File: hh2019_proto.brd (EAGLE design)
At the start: 250.5 x 149.7 mm, 145 parts, among them IC1 CP210X_USB_UART, IC2 AP2114H, IC4 TP4056, J1 PJ-313D, Q1 MMBT2222A, Q3 MMBT2222A, Q4 MMBT2222A, Q5 SI1304 BDL, U1 MPR121QR2, U2 ESP32-WROVER-I, U3 PCM5102A, X4 JST-PH3

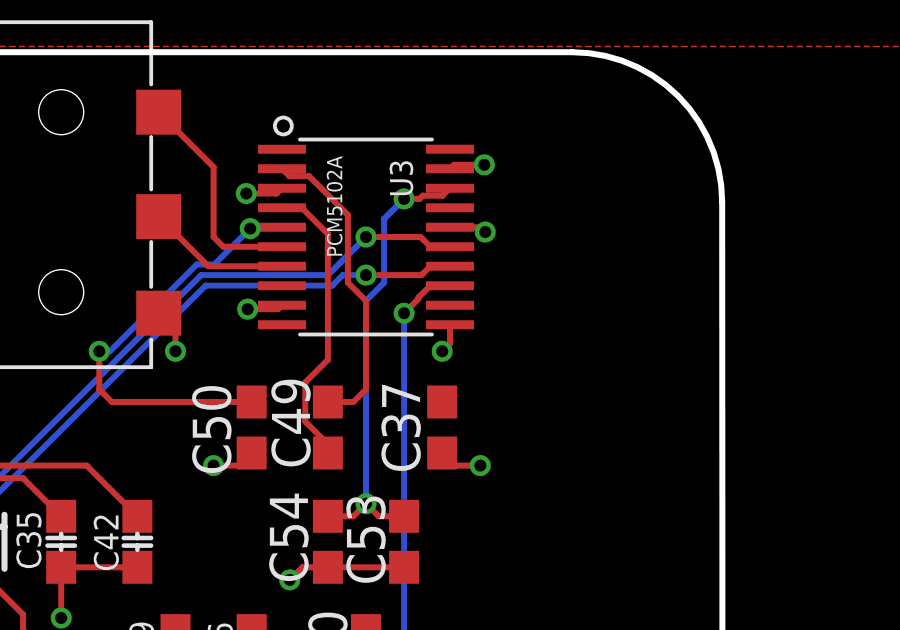
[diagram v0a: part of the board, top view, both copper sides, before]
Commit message: Fixed floating DAC pins being unconnected
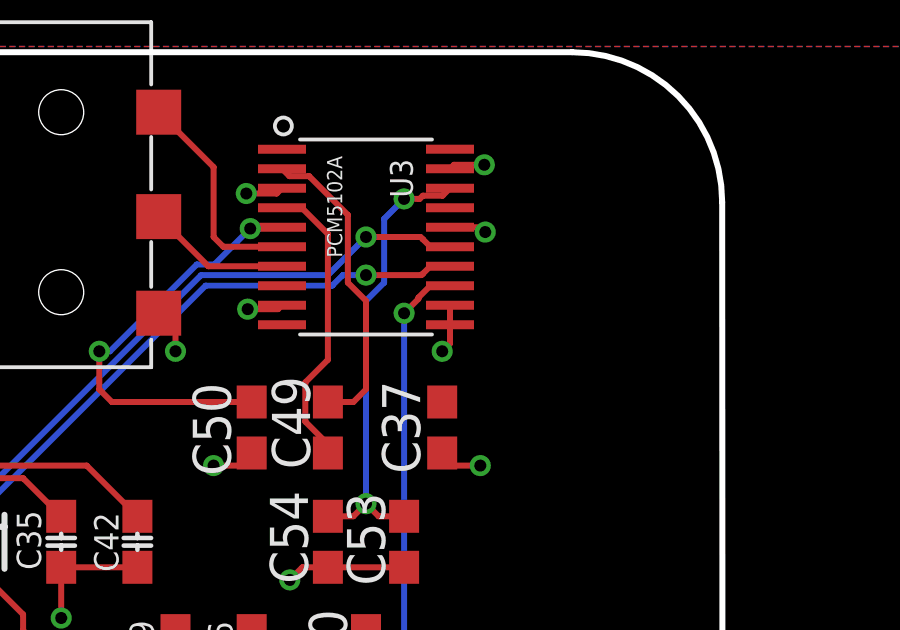
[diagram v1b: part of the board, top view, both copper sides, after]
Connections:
- removed net +3V3: U3.P$17
- removed net DEMP: U3.P$10
- net 3V3: now also U3.P$17
- net GND: now also U3.P$10
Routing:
- net GND: track 175.9 -> 176.6 mm
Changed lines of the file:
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@@
 <via x="-110.49" y="135.89" extent="1-16" drill="0.4"/>
 <contactref element="U3" pad="P$12"/>
+<wire x1="-93.72" y1="137.425" x2="-93.72" y2="136.775" width="0.2" layer="1"/>
+<contactref element="U3" pad="P$10"/>
 <wire x1="123.19" y1="72.39" x2="133.35" y2="72.39" width="0" layer="19" extent="1-1"/>
 <wire x1="114.3" y1="72.39" x2="123.19" y2="72.39" width="0" layer="19" extent="1-1"/>
@@
 <wire x1="104.14" y1="20.32" x2="114.3" y2="20.32" width="0" layer="19" extent="1-1"/>
 <wire x1="95.25" y1="20.32" x2="104.14" y2="20.32" width="0" layer="19" extent="1-1"/>
-<wire x1="-87.63" y1="68.58" x2="95.25" y2="72.39" width="0" layer="19" extent="1-1"/>
-<wire x1="-87.63" y1="76.2" x2="-87.63" y2="68.58" width="0" layer="19" extent="1-1"/>
-<wire x1="-87.593" y1="80.95" x2="-87.63" y2="76.2" width="0" layer="19" extent="1-1"/>
-<wire x1="-89.32" y1="86.36" x2="-88.9" y2="81.28" width="0" layer="19" extent="1-1"/>
-<wire x1="-87.593" y1="91.11" x2="-88.9" y2="87.63" width="0" layer="19" extent="1-1"/>
-<wire x1="-89.32" y1="96.52" x2="-88.9" y2="91.44" width="0" layer="19" extent="1-1"/>
-<wire x1="-87.593" y1="101.27" x2="-88.9" y2="97.79" width="0" layer="19" extent="1-1"/>
-<wire x1="-89.32" y1="106.68" x2="-88.9" y2="101.6" width="0" layer="19" extent="1-1"/>
-<wire x1="-96.47" y1="77.97" x2="-89.22" y2="76.2" width="0" layer="19" extent="1-1"/>
-<wire x1="-100.83" y1="78.77" x2="-99.06" y2="76.2" width="0" layer="19" extent="1-1"/>
-<wire x1="-100.4" y1="89.3" x2="-98.71" y2="86.44" width="0" layer="19" extent="1-1"/>
-<wire x1="-107.53" y1="90.17" x2="-102.84" y2="89.3" width="0" layer="19" extent="1-1"/>
-<wire x1="-113.88" y1="86.36" x2="-109.22" y2="90.17" width="0" layer="19" extent="1-1"/>
-<wire x1="-119.38" y1="91.44" x2="-113.88" y2="86.36" width="0" layer="19" extent="1-1"/>
-<wire x1="-99.06" y1="67.31" x2="-99.695" y2="75.565" width="0" layer="19" extent="1-1"/>
-<wire x1="-109.64" y1="63.5" x2="-99.06" y2="63.5" width="0" layer="19" extent="1-1"/>
-<wire x1="-114.046" y1="65.405" x2="-110.49" y2="64.77" width="0" layer="19" extent="1-1"/>
-<wire x1="-115.57" y1="57.47" x2="-110.04" y2="60.96" width="0" layer="19" extent="1-1"/>
-<wire x1="-118.11" y1="57.57" x2="-115.57" y2="57.47" width="0" layer="19" extent="1-1"/>
-<wire x1="-122.368240625" y1="49.15075625" x2="-118.11" y2="57.57" width="0" layer="19" extent="1-1"/>
-<wire x1="-118.91" y1="47.2" x2="-122.368240625" y2="49.15075625" width="0" layer="19" extent="1-1"/>
-<wire x1="-123.231115625" y1="42.646378125" x2="-123.49" y2="47.75" width="0" layer="19" extent="1-1"/>
-<wire x1="-124.206" y1="65.405" x2="-114.3" y2="65.659" width="0" layer="19" extent="1-1"/>
-<wire x1="-134.62" y1="98.21" x2="-123.16" y2="91.85" width="0" layer="19" extent="1-1"/>
-<wire x1="-140.34" y1="108.03" x2="-135.89" y2="98.21" width="0" layer="19" extent="1-1"/>
-<wire x1="-152.4" y1="107.95" x2="-140.34" y2="108.03" width="0" layer="19" extent="1-1"/>
-<wire x1="-152.4" y1="101.6" x2="-152.82" y2="106.68" width="0" layer="19" extent="1-1"/>
-<wire x1="-152.4" y1="97.79" x2="-151.093" y2="101.27" width="0" layer="19" extent="1-1"/>
-<wire x1="-152.4" y1="91.44" x2="-152.82" y2="96.52" width="0" layer="19" extent="1-1"/>
-<wire x1="-152.4" y1="87.63" x2="-151.093" y2="91.11" width="0" layer="19" extent="1-1"/>
-<wire x1="-152.4" y1="81.28" x2="-152.82" y2="86.36" width="0" layer="19" extent="1-1"/>
-<wire x1="-111.76" y1="108.827" x2="-111.76" y2="94.4" width="0" layer="19" extent="1-1"/>
-<wire x1="-122.56" y1="108.03" x2="-111.76" y2="108.827" width="0" layer="19" extent="1-1"/>
-<wire x1="-111.64" y1="121.92" x2="-110.49" y2="109.22" width="0" layer="19" extent="1-1"/>
-<wire x1="-110.49" y1="125.73" x2="-113.03" y2="123.61" width="0" layer="19" extent="1-1"/>
-<wire x1="-110.49" y1="128.4548" x2="-110.49" y2="125.73" width="0" layer="19" extent="1-1"/>
-<wire x1="-116.84" y1="128.69" x2="-114.3" y2="128.69" width="0" layer="19" extent="1-1"/>
-<wire x1="-106.68" y1="127" x2="-109.22" y2="124.88" width="0" layer="19" extent="1-1"/>
-<wire x1="-104.14" y1="124.46" x2="-106.68" y2="127" width="0" layer="19" extent="1-1"/>
-<wire x1="-99.06" y1="128.27" x2="-100.33" y2="124.88" width="0" layer="19" extent="1-1"/>
-<wire x1="-93.56" y1="132.08" x2="-95.25" y2="128.69" width="0" layer="19" extent="1-1"/>
-<wire x1="-93.98" y1="135.89" x2="-93.98" y2="132.5" width="0" layer="19" extent="1-1"/>
-<wire x1="-93.72" y1="137.425" x2="-93.72" y2="136.775" width="0" layer="19" extent="1-1"/>
-<wire x1="-93.72" y1="140.025" x2="-93.72" y2="137.425" width="0" layer="19" extent="1-1"/>
-<wire x1="-93.72" y1="141.975" x2="-93.72" y2="140.025" width="0" layer="19" extent="1-1"/>
-<wire x1="-100.75" y1="132.08" x2="-98.64" y2="128.69" width="0" layer="19" extent="1-1"/>
-<wire x1="-102.87" y1="135.89" x2="-101.6" y2="132.08" width="0" layer="19" extent="1-1"/>
-<wire x1="-100.464446875" y1="137.294446875" x2="-102.87" y2="136.6" width="0" layer="19" extent="1-1"/>
-<wire x1="-99.495553125" y1="141.149446875" x2="-99.32" y2="137.425" width="0" layer="19" extent="1-1"/>
-<wire x1="-102.87" y1="119.7" x2="-103.29" y2="124.46" width="0" layer="19" extent="1-1"/>
-<wire x1="-119.93" y1="133.99" x2="-119.38" y2="128.69" width="0" layer="19" extent="1-1"/>
-<wire x1="-124.43" y1="133.99" x2="-119.93" y2="133.99" width="0" layer="19" extent="1-1"/>
-<wire x1="-109.93" y1="137.16" x2="-103.43" y2="137.16" width="0" layer="19" extent="1-1"/>
-<wire x1="-133.9076" y1="132.60455" x2="-124.43" y2="133.99" width="0" layer="19" extent="1-1"/>
-<wire x1="-142.24" y1="128.69" x2="-137.16" y2="133.35" width="0" layer="19" extent="1-1"/>
-<wire x1="-146.05" y1="127.42" x2="-142.24" y2="128.69" width="0" layer="19" extent="1-1"/>
-<wire x1="-146.05" y1="139.58" x2="-146.05" y2="132.4" width="0" layer="19" extent="1-1"/>
-<wire x1="-142.24" y1="143.51" x2="-146.05" y2="140.97" width="0" layer="19" extent="1-1"/>
-<wire x1="-134.25" y1="141.89" x2="-138.05" y2="141.09" width="0" layer="19" extent="1-1"/>
+<wire x1="-87.63" y1="76.2" x2="95.25" y2="72.39" width="0" layer="19" extent="1-1"/>
+<wire x1="-99.32" y1="136.775" x2="-99.450553125" y2="137.294446875" width="0" layer="19" extent="1-1"/>
 </signal>
 <signal name="USB_DN_CON">
@@
 <wire x1="-112.71" y1="59.37" x2="-107.95" y2="54.61" width="0.2" layer="1"/>
 <wire x1="-107.95" y1="54.61" x2="-104.14" y2="54.61" width="0.2" layer="1"/>
+<contactref element="U3" pad="P$17"/>
 </signal>
 <signal name="GDR">
@@
 <wire x1="-104.99" y1="134.2" x2="-100.33" y2="134.2" width="0.2" layer="1"/>
 </signal>
-<signal name="DEMP" class="2">
-<contactref element="U3" pad="P$10"/>
-</signal>
 <signal name="BAT" class="1">
 <contactref element="X4" pad="3"/>
@@
 <wire x1="-106.045" y1="76.835" x2="-107.175" y2="76.835" width="0.2" layer="1"/>
 </signal>
-<signal name="+3V3">
-<contactref element="U3" pad="P$17"/>
-</signal>
 </signals>

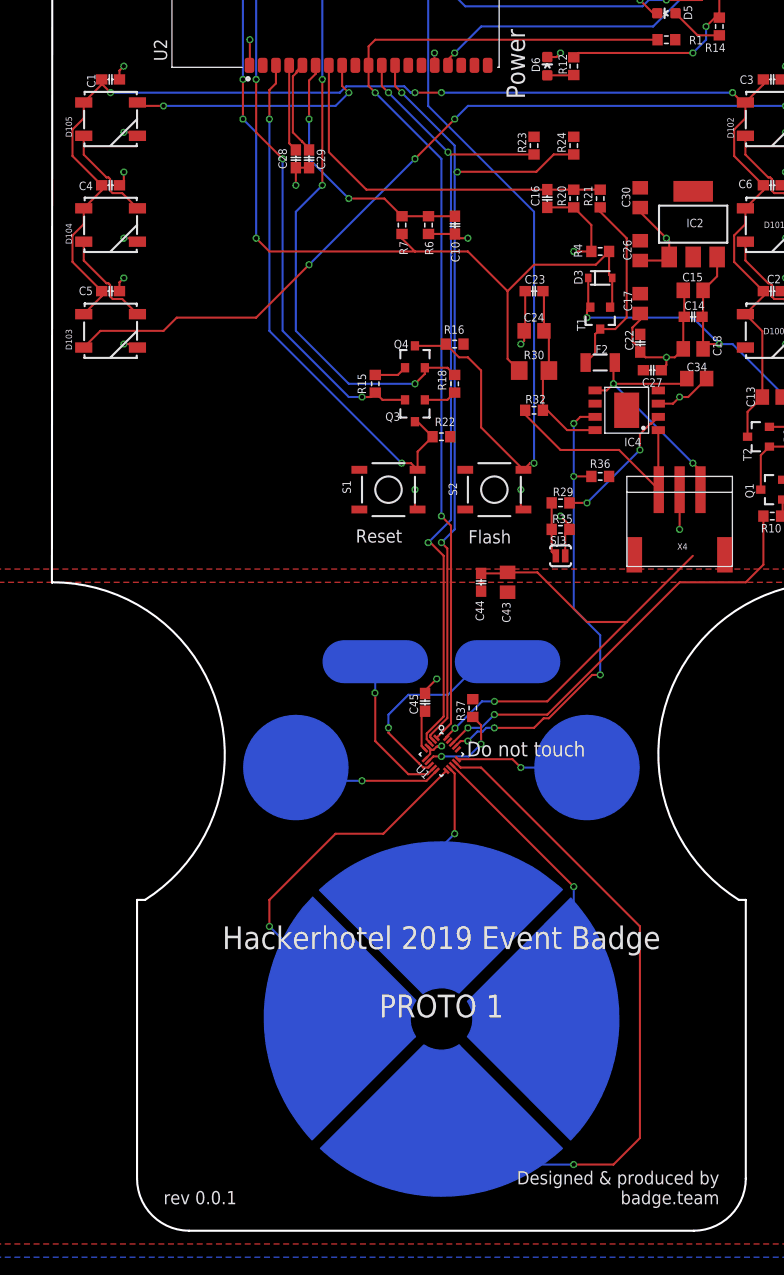
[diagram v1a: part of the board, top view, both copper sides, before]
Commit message: Increased touch trace robustness, and added proper passthrough of back groundplane
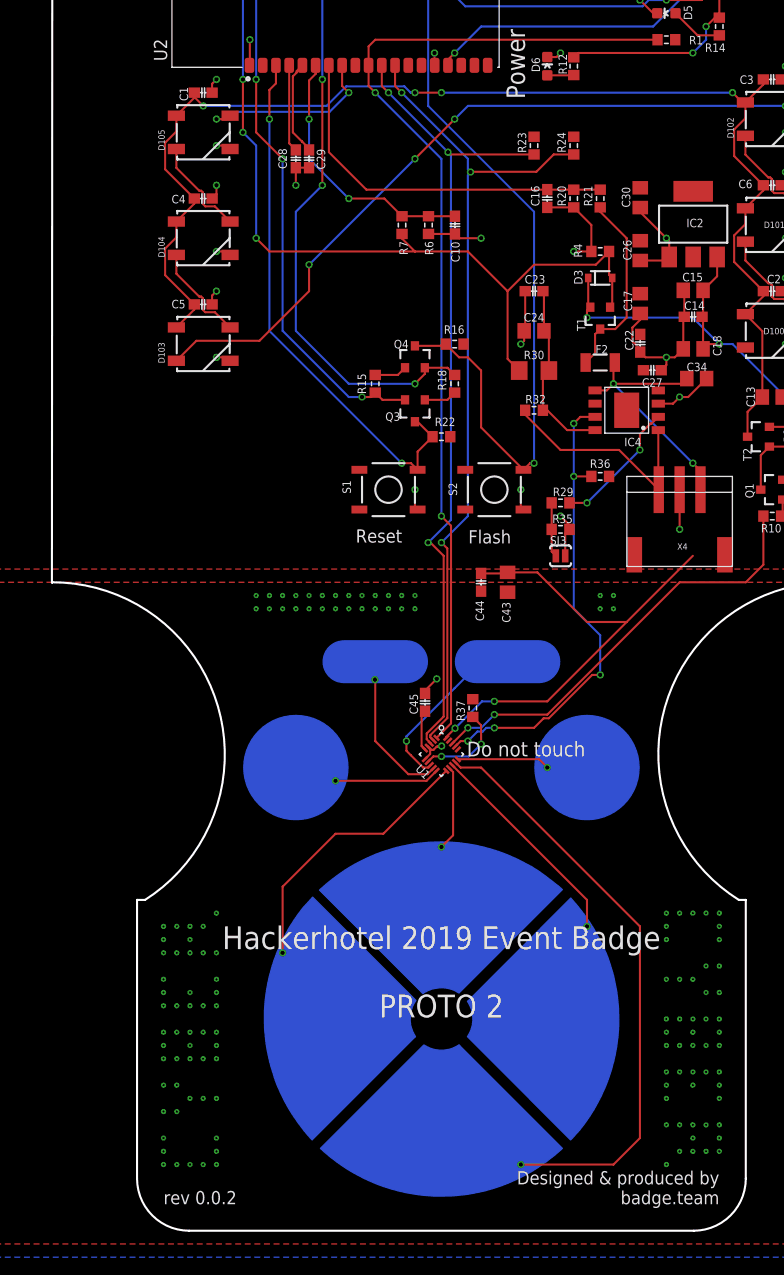
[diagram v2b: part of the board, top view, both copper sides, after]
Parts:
- moved C1 8.98 mm to (-144.8, 105.4)
- moved D105 8.98 mm to (-144.8, 101.6)
- moved C4 8.98 mm to (-144.8, 95.2)
- moved C5 8.98 mm to (-144.8, 85.1)
- moved D103 8.98 mm to (-144.8, 81.3)
- moved D104 8.98 mm to (-144.8, 91.4)
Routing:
- net WS2812_POWER: track 132.2 -> 123.9 mm
- net N$50: track 78.4 -> 71.5 mm
- net WS2812_DATA: track 23.8 -> 18.5 mm
- net ELE0: track 20.4 -> 16.7 mm
- net GND: track 176.6 -> 177.9 mm
- net ELE3: track 35.6 -> 34.6 mm
- net ELE5: track 30.9 -> 31.9 mm
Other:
- board text added: "Hackerhotel 2019 Event Badge PROTO 2"
- board text added: "rev 0.0.2"
- board text removed: "Hackerhotel 2019 Event Badge PROTO 1"
- board text removed: "rev 0.0.1"

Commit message: Made board smaller, placed caps closer to touch controller, increased free space around display connector, implemented dull brick PCB design. Fixes issues #2 #3 #4.
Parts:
- moved C40 16.7 mm to (-109.5, 115.2)
- moved C39 15.7 mm to (-114.5, 115.2)
- moved C46 15.7 mm to (-112.0, 115.2)
- moved R4 14.0 mm to (-120.7, 90.2)
- moved U3 11.4 mm to (-100.6, 129.0)
- moved C37 10.9 mm to (-97.8, 123.2)
- moved C50 10.5 mm to (-102.9, 123.2)
- moved C53 10.5 mm to (-97.8, 119.4)
- moved C54 10.5 mm to (-100.3, 119.4)
- moved C44 10.2 mm to (-115.4, 48.6), turned to 90 degrees
- moved C14 10.2 mm to (-107.9, 83.9)
- moved C15 10.2 mm to (-107.9, 86.4)
- moved C16 10.2 mm to (-121.9, 95.2)
- moved C17 10.2 mm to (-113.0, 85.2)
- moved C18 10.2 mm to (-107.9, 80.8)
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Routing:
- net +5V: track 126.8 -> 112.5 mm
- net I2S_SCK: track 51.5 -> 37.7 mm
- net GND: track 177.9 -> 191.2 mm, vias 56 -> 53
- net AUDIO_L: track 7.33 -> 20.5 mm
- net AUDIO_R: track 4.80 -> 16.5 mm
- net VBAT_SENSE: track 35.9 -> 25.7 mm
- net WS2812_POWER: track 123.9 -> 114.9 mm
- net N$50: track 71.5 -> 62.8 mm
- net WS2812_POWER_EN: track 41.7 -> 33.0 mm
- net I2S_SD: track 37.9 -> 29.4 mm
- net I2S_WS: track 36.6 -> 28.2 mm
- net VDD: track 89.7 -> 81.5 mm
- net CAPP: track 10.3 -> 3.36 mm
- net VCC: track 43.8 -> 50.4 mm
- net I2C_SCL: track 80.6 -> 74.3 mm
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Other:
- board size 250.5 x 149.7 mm -> 242.3 x 153.7 mm

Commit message: Finished PCB design. Added Shitty AddOn, IR, buzzer
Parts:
- removed $$U$1, $$U$2, $$U$3, $$U$4, $$U$5, $$U$6, $$U$7, $$U$8, $$U$9, U$10, U$11, U$12, U$13, U$14, U$15, U$16, U$17, U$18, U$19, U$2, U$20, U$21, U$22, U$23, U$3, U$4, U$5, U$6: VIA, badge:VIA
- removed FD2, FD3: FIDUCIAL, adafruit:FIDUCIAL_1MM
- added IR_R: (no value), pinhead:1X03
- added JP1: JUMPER-SMT_2_NC_TRACE_SILK, SparkFun-Jumpers:SMT-JUMPER_2_NC_TRACE_SILK
- added JP2: (no value), pinhead:1X02
- added LED1: (no value), led:LED5MM
- added Q2: (no value), transistor-power:SO-08
- added R2, R5: 10k, hh2019_proto:R0603-DASHES
- added SHITTY-ADDON: (no value), pinhead:2X02
- moved C11 227.7 mm to (80.5, 151.4), flipped to the bottom
- moved C9 227.7 mm to (80.5, 156.5), flipped to the bottom
- moved D1 227.7 mm to (80.5, 161.5), flipped to the bottom
- moved C1 225.2 mm to (79.2, 128.5), flipped to the bottom
- moved C4 225.2 mm to (79.2, 118.4), flipped to the bottom
- moved C5 225.2 mm to (79.2, 108.2), flipped to the bottom
- moved D103 225.2 mm to (79.2, 104.4), flipped to the bottom
- moved D104 225.2 mm to (79.2, 114.6), flipped to the bottom
- moved D105 225.2 mm to (79.2, 124.7), flipped to the bottom
- moved C8 220.1 mm to (76.6, 152.7), flipped to the bottom
- moved F1 220.1 mm to (76.6, 160.3), flipped to the bottom
- moved R13 220.1 mm to (76.6, 156.5), flipped to the bottom
- moved USB1 214.2 mm to (73.7, 167.3), flipped to the bottom
- moved IC1 210.0 mm to (71.6, 156.5), flipped to the bottom
- moved C28 207.5 mm to (70.3, 122.2), flipped to the bottom
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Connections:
- new net BUZZER: Q2.4, U2.26
- new net BUZZ_OUT: JP2.1, Q2.5, Q2.6, Q2.7, Q2.8
- new net ESP32_TX_PRE: JP1.1, R2.2, U2.35
- new net IR_RECV: IR_R.1, R5.2, U2.14
- new net IR_SEND: LED1.A, U2.13
- net 3V3: now also IR_R.3, JP2.2, R5.1, SHITTY-ADDON.2
- net ESP32_TX: now also JP1.2, R2.1; no longer U2.35
- net GND: now also IR_R.2, LED1.K, Q2.1, Q2.2, Q2.3, SHITTY-ADDON.1; no longer $$U$1.P$1, $$U$2.P$1, $$U$3.P$1, $$U$4.P$1, $$U$5.P$1, $$U$6.P$1, $$U$7.P$1, $$U$8.P$1, $$U$9.P$1, U$10.P$1, U$11.P$1, U$12.P$1, U$13.P$1, U$14.P$1, U$15.P$1, U$16.P$1, U$17.P$1, U$18.P$1, U$19.P$1, U$2.P$1, U$20.P$1, U$21.P$1, U$22.P$1, U$23.P$1, U$3.P$1, U$4.P$1, U$5.P$1, U$6.P$1
- net I2C_SCL: now also SHITTY-ADDON.3
- net I2C_SDA: now also SHITTY-ADDON.4
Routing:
- net BUZZER: track 0.00 -> 73.3 mm, vias 0 -> 6
- net IR_RECV: track 0.00 -> 56.7 mm, vias 0 -> 2
- net IR_SEND: track 0.00 -> 43.3 mm, vias 0 -> 2
- net I2C_SCL: track 74.3 -> 108.8 mm, vias 3 -> 6
- net I2C_SDA: track 72.3 -> 103.3 mm, vias 3 -> 6
- net GND: track 191.2 -> 205.1 mm
- net ESP32_TX_PRE: track 0.00 -> 11.3 mm, vias 0 -> 2
- net BUZZ_OUT: track 0.00 -> 7.30 mm
- net ESP32_TX: track 43.6 -> 49.6 mm, vias 2 -> 4
- net WS2812_POWER_EN: track 33.0 -> 37.0 mm
- net 3V3: track 43.4 -> 47.2 mm, vias 2 -> 3
- net LDO0: track 16.0 -> 19.8 mm
- net ELE0: track 20.3 -> 23.8 mm, vias 1 -> 3
- net VCC: track 50.4 -> 49.4 mm
- net LCD_!RESET: track 21.6 -> 20.9 mm
- added copper zone on layer 16, net 3V3
- removed copper zone on layer 1, net 3V3
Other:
- board size 242.3 x 153.7 mm -> 80.8 x 165.7 mm
- board text added: "3V3"
- board text added: "IR_RECV"
- board text added: "SCL"
- board text added: "SDA"
- board text removed: "5V"
- board text removed: "RX"
- board text removed: "TX"
- board text removed: "USB"
- board text removed: "USB_DN_CON"
- board text removed: "USB_DP_CON"
- board text removed: "VBAT"
- board text removed: "VUSB_IN"
